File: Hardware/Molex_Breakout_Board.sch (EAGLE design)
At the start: 13 parts

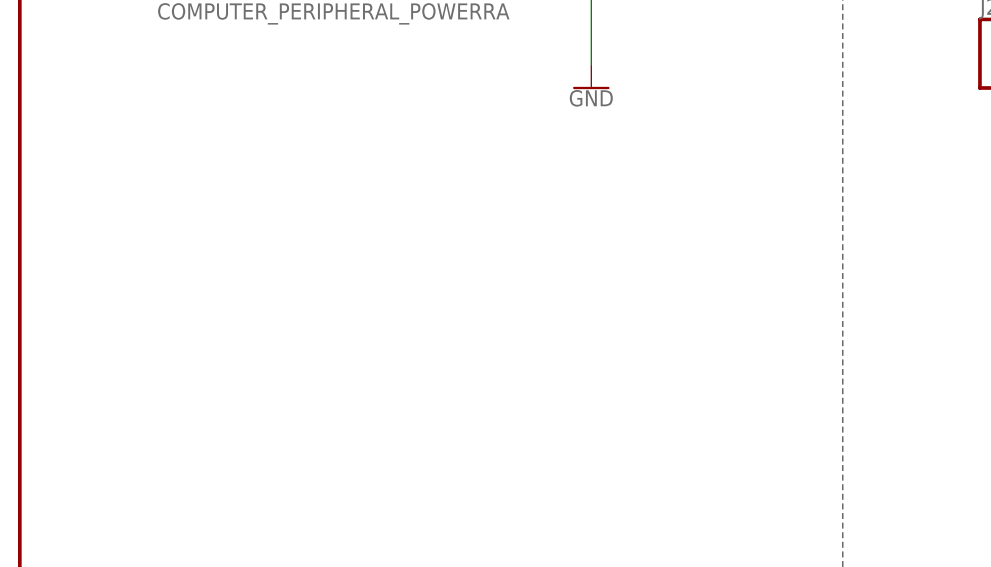
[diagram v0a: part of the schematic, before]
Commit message: Update Molex_Breakout_Board.sch
- Add Note for vertical mount molex connector
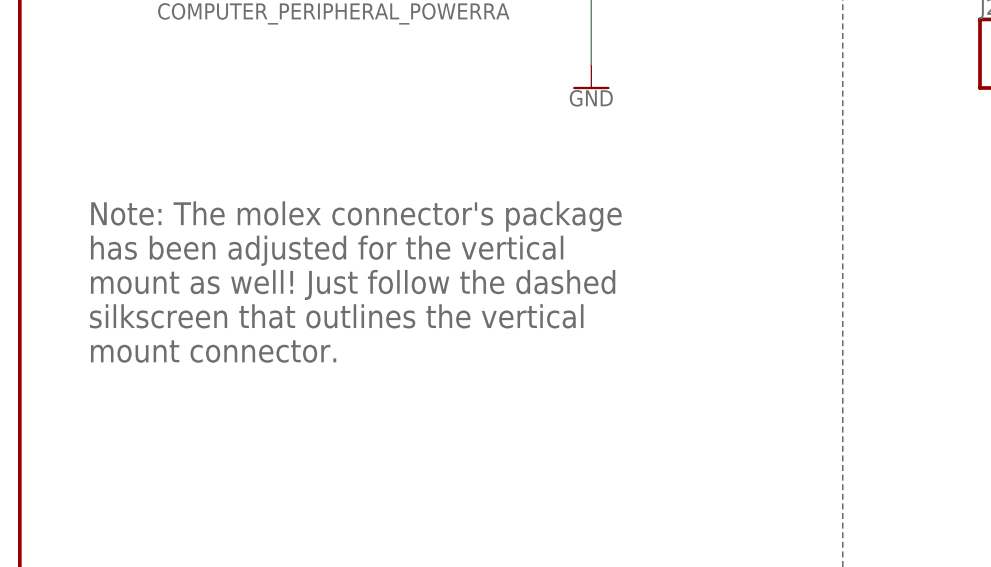
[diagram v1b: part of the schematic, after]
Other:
- note added: "Note: The molex connector's package has been adjusted for the vertical mount as well! Just follow the dashed silkscreen that outlines the vertical mount connector."
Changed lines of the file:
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@@
 <grid distance="0.1" unitdist="inch" unit="inch" style="lines" multiple="1" display="no" altdistance="0.01" altunitdist="inch" altunit="inch"/>
 <layers>
-<layer number="1" name="Top" color="4" fill="1" visible="yes" active="no"/>
-<layer number="16" name="Bottom" color="1" fill="1" visible="yes" active="no"/>
-<layer number="17" name="Pads" color="2" fill="1" visible="yes" active="no"/>
-<layer number="18" name="Vias" color="2" fill="1" visible="yes" active="no"/>
-<layer number="19" name="Unrouted" color="6" fill="1" visible="yes" active="no"/>
-<layer number="20" name="Dimension" color="15" fill="1" visible="yes" active="no"/>
-<layer number="21" name="tPlace" color="16" fill="1" visible="yes" active="no"/>
-<layer number="22" name="bPlace" color="14" fill="1" visible="yes" active="no"/>
-<layer number="23" name="tOrigins" color="15" fill="1" visible="yes" active="no"/>
-<layer number="24" name="bOrigins" color="15" fill="1" visible="yes" active="no"/>
-<layer number="25" name="tNames" color="7" fill="1" visible="yes" active="no"/>
-<layer number="26" name="bNames" color="7" fill="1" visible="yes" active="no"/>
-<layer number="27" name="tValues" color="7" fill="1" visible="yes" active="no"/>
-<layer number="28" name="bValues" color="7" fill="1" visible="yes" active="no"/>
+<layer number="1" name="Top" color="4" fill="1" visible="no" active="no"/>
+<layer number="16" name="Bottom" color="1" fill="1" visible="no" active="no"/>
+<layer number="17" name="Pads" color="2" fill="1" visible="no" active="no"/>
+<layer number="18" name="Vias" color="2" fill="1" visible="no" active="no"/>
+<layer number="19" name="Unrouted" color="6" fill="1" visible="no" active="no"/>
+<layer number="20" name="Dimension" color="15" fill="1" visible="no" active="no"/>
+<layer number="21" name="tPlace" color="16" fill="1" visible="no" active="no"/>
+<layer number="22" name="bPlace" color="14" fill="1" visible="no" active="no"/>
+<layer number="23" name="tOrigins" color="15" fill="1" visible="no" active="no"/>
+<layer number="24" name="bOrigins" color="15" fill="1" visible="no" active="no"/>
+<layer number="25" name="tNames" color="7" fill="1" visible="no" active="no"/>
+<layer number="26" name="bNames" color="7" fill="1" visible="no" active="no"/>
+<layer number="27" name="tValues" color="7" fill="1" visible="no" active="no"/>
+<layer number="28" name="bValues" color="7" fill="1" visible="no" active="no"/>
 <layer number="29" name="tStop" color="7" fill="3" visible="no" active="no"/>
 <layer number="30" name="bStop" color="7" fill="6" visible="no" active="no"/>
@@
 <layer number="35" name="tGlue" color="7" fill="4" visible="no" active="no"/>
 <layer number="36" name="bGlue" color="7" fill="5" visible="no" active="no"/>
-<layer number="37" name="tTest" color="7" fill="1" visible="yes" active="no"/>
-<layer number="38" name="bTest" color="7" fill="1" visible="yes" active="no"/>
+<layer number="37" name="tTest" color="7" fill="1" visible="no" active="no"/>
+<layer number="38" name="bTest" color="7" fill="1" visible="no" active="no"/>
 <layer number="39" name="tKeepout" color="4" fill="11" visible="no" active="no"/>
 <layer number="40" name="bKeepout" color="1" fill="11" visible="no" active="no"/>
@@
 <layer number="44" name="Drills" color="7" fill="1" visible="no" active="no"/>
 <layer number="45" name="Holes" color="7" fill="1" visible="no" active="no"/>
-<layer number="46" name="Milling" color="3" fill="1" visible="yes" active="no"/>
-<layer number="47" name="Measures" color="7" fill="1" visible="yes" active="no"/>
-<layer number="48" name="Document" color="7" fill="1" visible="yes" active="no"/>
-<layer number="49" name="Reference" color="7" fill="1" visible="yes" active="no"/>
-<layer number="50" name="dxf" color="7" fill="1" visible="yes" active="no"/>
-<layer number="51" name="tDocu" color="6" fill="1" visible="yes" active="no"/>
-<layer number="52" name="bDocu" color="7" fill="1" visible="yes" active="no"/>
-<layer number="53" name="tGND_GNDA" color="7" fill="9" visible="yes" active="no"/>
-<layer number="54" name="bGND_GNDA" color="1" fill="9" visible="yes" active="no"/>
-<layer number="56" name="wert" color="7" fill="1" visible="yes" active="no"/>
-<layer number="57" name="tCAD" color="7" fill="1" visible="yes" active="no"/>
-<layer number="59" name="tCarbon" color="7" fill="1" visible="yes" active="no"/>
-<layer number="60" name="bCarbon" color="7" fill="1" visible="yes" active="no"/>
+<layer number="46" name="Milling" color="3" fill="1" visible="no" active="no"/>
+<layer number="47" name="Measures" color="7" fill="1" visible="no" active="no"/>
+<layer number="48" name="Document" color="7" fill="1" visible="no" active="no"/>
+<layer number="49" name="Reference" color="7" fill="1" visible="no" active="no"/>
+<layer number="50" name="dxf" color="7" fill="1" visible="no" active="no"/>
+<layer number="51" name="tDocu" color="6" fill="1" visible="no" active="no"/>
+<layer number="52" name="bDocu" color="7" fill="1" visible="no" active="no"/>
+<layer number="53" name="tGND_GNDA" color="7" fill="9" visible="no" active="no"/>
+<layer number="54" name="bGND_GNDA" color="1" fill="9" visible="no" active="no"/>
+<layer number="56" name="wert" color="7" fill="1" visible="no" active="no"/>
+<layer number="57" name="tCAD" color="7" fill="1" visible="no" active="no"/>
+<layer number="59" name="tCarbon" color="7" fill="1" visible="no" active="no"/>
+<layer number="60" name="bCarbon" color="7" fill="1" visible="no" active="no"/>
 <layer number="88" name="SimResults" color="9" fill="1" visible="yes" active="yes"/>
 <layer number="89" name="SimProbes" color="9" fill="1" visible="yes" active="yes"/>
@@
 <wire x1="147.32" y1="116.84" x2="147.32" y2="35.56" width="0.1524" layer="97" style="shortdash"/>
 <wire x1="147.32" y1="116.84" x2="248.92" y2="116.84" width="0.1524" layer="97" style="shortdash"/>
+<text x="7.62" y="63.5" size="2.54" layer="95" font="vector" ratio="15">Note: The molex connector's package
+has been adjusted for the vertical
+mount as well! Just follow the dashed
+silkscreen that outlines the vertical
+mount connector.</text>
 </plain>
 <instances>
@@
 </schematic>
 </drawing>
+<compatibility>
+<note version="6.3" minversion="6.2.2" severity="warning">
+Since Version 6.2.2 text objects can contain more than one line,
+which will not be processed correctly with this version.
+</note>
+</compatibility>
 </eagle>
